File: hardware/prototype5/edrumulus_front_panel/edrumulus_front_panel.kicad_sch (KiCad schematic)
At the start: 8 parts, among them J2 Raspberry Pi GPIO pins, SW1 SW_Push, SW2 SW_Push, SW3 SW_Push, SW4 SW_Push, SW5 SW_Push, SW6 SW_Push

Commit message: some more work for the display hat for prototype 5
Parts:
- added R?: R, symbol Device:R
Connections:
- net PI-GPIO17: now reaches J2.11 (Pin_11)
- net PI-GPIO17: now also DS1.6 (E)
- net PI-GPIO27: now reaches J2.13 (Pin_13)
- net PI-GPIO27: now also DS1.4 (RS)
- net PI-GPIO22: now reaches J2.15 (Pin_15)
- net PI-GPIO22: now also DS1.11 (D4)
- net PI-GPIO23: now reaches J2.16 (Pin_16)
- net PI-GPIO23: now also DS1.12 (D5)
- net PI-GPIO24: now reaches J2.18 (Pin_18)
- net PI-GPIO24: now also DS1.13 (D6)
- net PI-GPIO10: now reaches J2.19 (Pin_19)
- net PI-GPIO10: now also DS1.14 (D7)
- net PI-GPIO25: now reaches J2.22 (Pin_22)
- net PI-GPIO11: now reaches J2.23 (Pin_23)
- net PI-GPIO8: now reaches J2.24 (Pin_24)
- net PI-GPIO7: now reaches J2.26 (Pin_26)
- net PI-GPIO12: now reaches J2.32 (Pin_32)
- net PI-GPIO13: now reaches J2.33 (Pin_33)
- net ESP-UART0-RX: no longer names the net of J2.8 (Pin_8)
- net ESP-UART0-TX: no longer names the net of J2.10 (Pin_10)
- net PI-GPIO4: no longer names the net of J2.7 (Pin_7)
- net PI-GPIO9: no longer names the net of J2.21 (Pin_21)
- no-connect marks 27 -> 19

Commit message: work on display for prototype 5
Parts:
- added R10, R12, R2, R4, R6, R8: 1k, Resistor_SMD:R_1206_3216Metric_Pad1.30x1.75mm_HandSolder, symbol Device:R
- added R11, R3, R5, R7, R9: 10k, Resistor_SMD:R_1206_3216Metric_Pad1.30x1.75mm_HandSolder, symbol Device:R
- added R13: 470, Resistor_SMD:R_1206_3216Metric_Pad1.30x1.75mm_HandSolder, symbol Device:R
- added RV1: 10k, Potentiometer_THT:Potentiometer_ACP_CA9-H2,5_Horizontal, symbol Device:R_Potentiometer
- R1: renamed from R?; value R -> 10k; footprint (none) -> Resistor_SMD:R_1206_3216Metric_Pad1.30x1.75mm_HandSolder
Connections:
- net RASPI-VIN is gone; now on net 5V: J2.2 (Pin_2), J2.4 (Pin_4)
- net GND: now also DS1.1 (VSS), DS1.16 (LED(-)), DS1.5 (R/W), SW1.2, SW2.2, SW3.2, SW4.2, SW5.2, SW6.2, RV1.1
- net PI-GPIO11: now also R4.2
- net PI-GPIO12: now also R10.2
- net PI-GPIO13: now also R12.2
- net PI-GPIO25: now also R2.2
- net PI-GPIO7: now also R8.2
- net PI-GPIO8: now also R6.2
- net 3V3: now reaches J2.1 (Pin_1)
- net 3V3: now also R1.1, R11.1, R3.1, R5.1, R7.1, R9.1
- net at SW4.1: now also R7.2, R8.1
- net at SW5.1: now also R10.1, R9.2
- net at SW2.1: now also R3.2, R4.1
- net at SW1.1: now also R1.2, R2.1
- net at SW3.1: now also R5.2, R6.1
- net at SW6.1: now also R11.2, R12.1
- net at DS1.15 (LED(+)): now also R13.1
- net 5V: now reaches DS1.2 (VDD)
- net 5V: now also R13.2, RV1.3
- net at DS1.3 (VO): now also RV1.2
- no-connect marks 19 -> 22
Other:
- moved on the sheet: DS1, R1, SW1

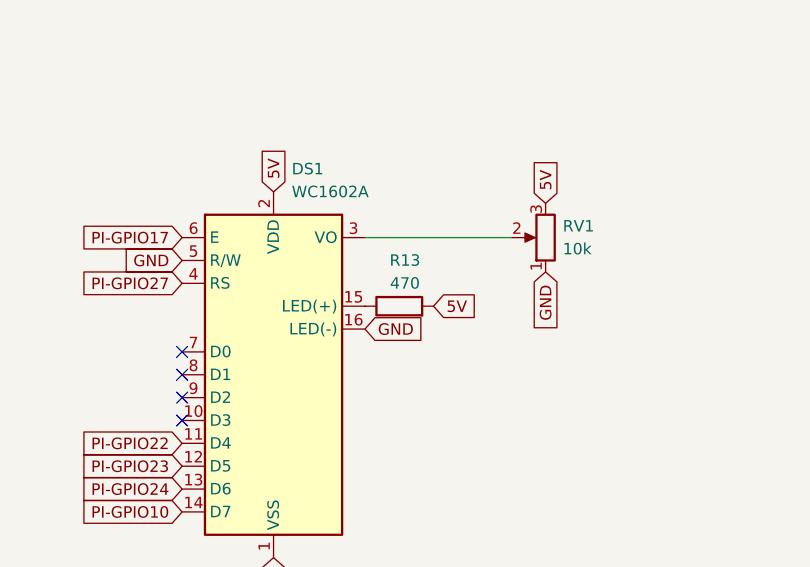
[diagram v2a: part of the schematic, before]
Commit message: fixes for the front panel for prototype 5
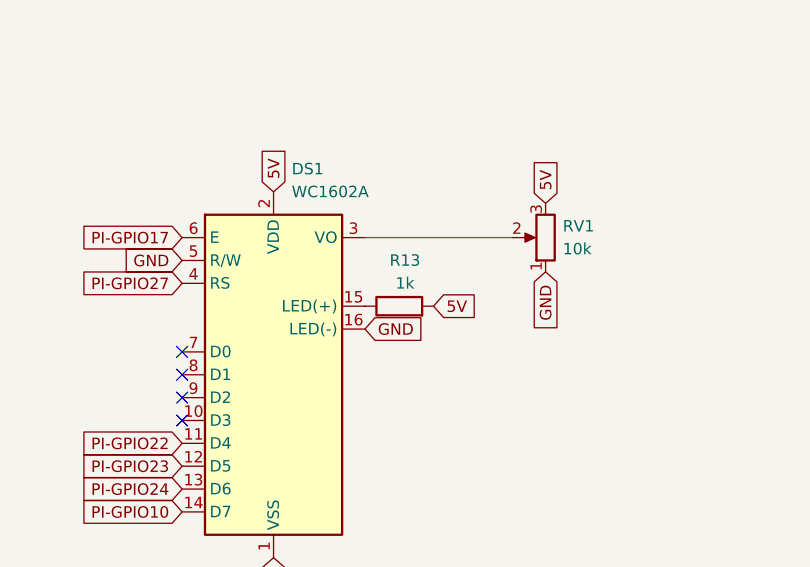
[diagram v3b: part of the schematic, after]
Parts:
- R13: value 470 -> 1k
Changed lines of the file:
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@@
     (in_bom yes) (on_board yes)
     (property "Reference" "R13" (id 0) (at 92.075 85.598 90))
-    (property "Value" "470" (id 1) (at 92.075 88.138 90))
+    (property "Value" "1k" (id 1) (at 92.075 88.138 90))
     (property "Footprint" "Resistor_SMD:R_1206_3216Metric_Pad1.30x1.75mm_HandSolder" (id 2) (at 91.44 92.456 90)
       (effects (font (size 1.27 1.27)) hide)
@@
     )
     (path "/7a4fc15d-3e02-4709-96a9-8c72ac60b42a"
-      (reference "R13") (unit 1) (value "470") (footprint "Resistor_SMD:R_1206_3216Metric_Pad1.30x1.75mm_HandSolder")
+      (reference "R13") (unit 1) (value "1k") (footprint "Resistor_SMD:R_1206_3216Metric_Pad1.30x1.75mm_HandSolder")
     )
     (path "/1c5e8fb0-f2a2-4d47-ad22-c6702a176120"
